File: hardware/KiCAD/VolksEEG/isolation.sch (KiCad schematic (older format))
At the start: 3 parts

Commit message: Added debugging bits to more schematic sheets.
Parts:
- added C? (x5): 100n, symbol Device:C
- added D?: Blue, symbol Device:LED
- added D?: Green, symbol Device:LED
- added R?: 220R, symbol Device:R
- added R?: 330R, symbol Device:R
- added TP? (x3): GNDD_tp, symbol Connector:TestPoint
- added TP?: ADS_nDRDY_tp, symbol Connector:TestPoint
- added TP?: ADS_nDRDY_ni_tp, symbol Connector:TestPoint
- added TP?: MISO_ni_tp, symbol Connector:TestPoint
- added TP?: SCK_tp, symbol Connector:TestPoint
- added TP?: SCK_ni_tp, symbol Connector:TestPoint
- added TP?: nCS_tp, symbol Connector:TestPoint
- added TP?: ADS_nRST_tp, symbol Connector:TestPoint
- added TP?: MOSI_tp, symbol Connector:TestPoint
- added TP?: nCS_ni_tp, symbol Connector:TestPoint
- added TP?: ADS_nRST_ni_tp, symbol Connector:TestPoint
- added TP?: MOSI_ni_tp, symbol Connector:TestPoint
- added TP?: 5V_tp, symbol Connector:TestPoint
- added TP?: MISO_tp, symbol Connector:TestPoint
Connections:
- wire segments 48 -> 96

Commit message: Changed ADuM420 sch symbol to more KiCAD-like look.
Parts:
- removed C? (x2): 100n, symbol Device:C
- removed TP?: ADS_nDRDY_tp, symbol Connector:TestPoint
- removed TP?: ADS_nDRDY_ni_tp, symbol Connector:TestPoint
- removed TP?: MISO_ni_tp, symbol Connector:TestPoint
- removed TP?: MISO_tp, symbol Connector:TestPoint
- removed U? (x2): ADUM240E1BRIZ-RL, RI_16_2_ADI, symbol VolksEEG:ADUM240E1BRIZ-RL
- added C? (x2): 100n, symbol Device:C
- added TP?: ADS_nRST_tp, symbol Connector:TestPoint
- added TP?: MOSI_tp, symbol Connector:TestPoint
- added TP?: ADS_nRST_ni_tp, symbol Connector:TestPoint
- added TP?: MOSI_ni_tp, symbol Connector:TestPoint
- added U? (x2): ADUM240E1BRIZ-RL, RI_16_2_ADI, symbol VolksEEG:ADUM240E1BRIZ-RL
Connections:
- wire segments 96 -> 104
- no-connect marks 0 -> 4
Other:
- moved on the sheet: C?, TP?

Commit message: Changed MEJ1S sch symbol to be more KiCAD-like.
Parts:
- removed U?: MEJ1S0305SC, MEJ1_SINGLE_SIP_MUR, symbol MEJ1S0305SC:MEJ1S0305SC
- added U?: MEJ1S0305SC, MEJ1_SINGLE_SIP_MUR, symbol VolksEEG:MEJ1S0305SC
- C?: symbol Device:C -> Device:C_Small
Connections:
- wire segments 104 -> 106
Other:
- note added: "5V Boost Converter\n(Isolation)"
- moved on the sheet: C?, TP?, U?

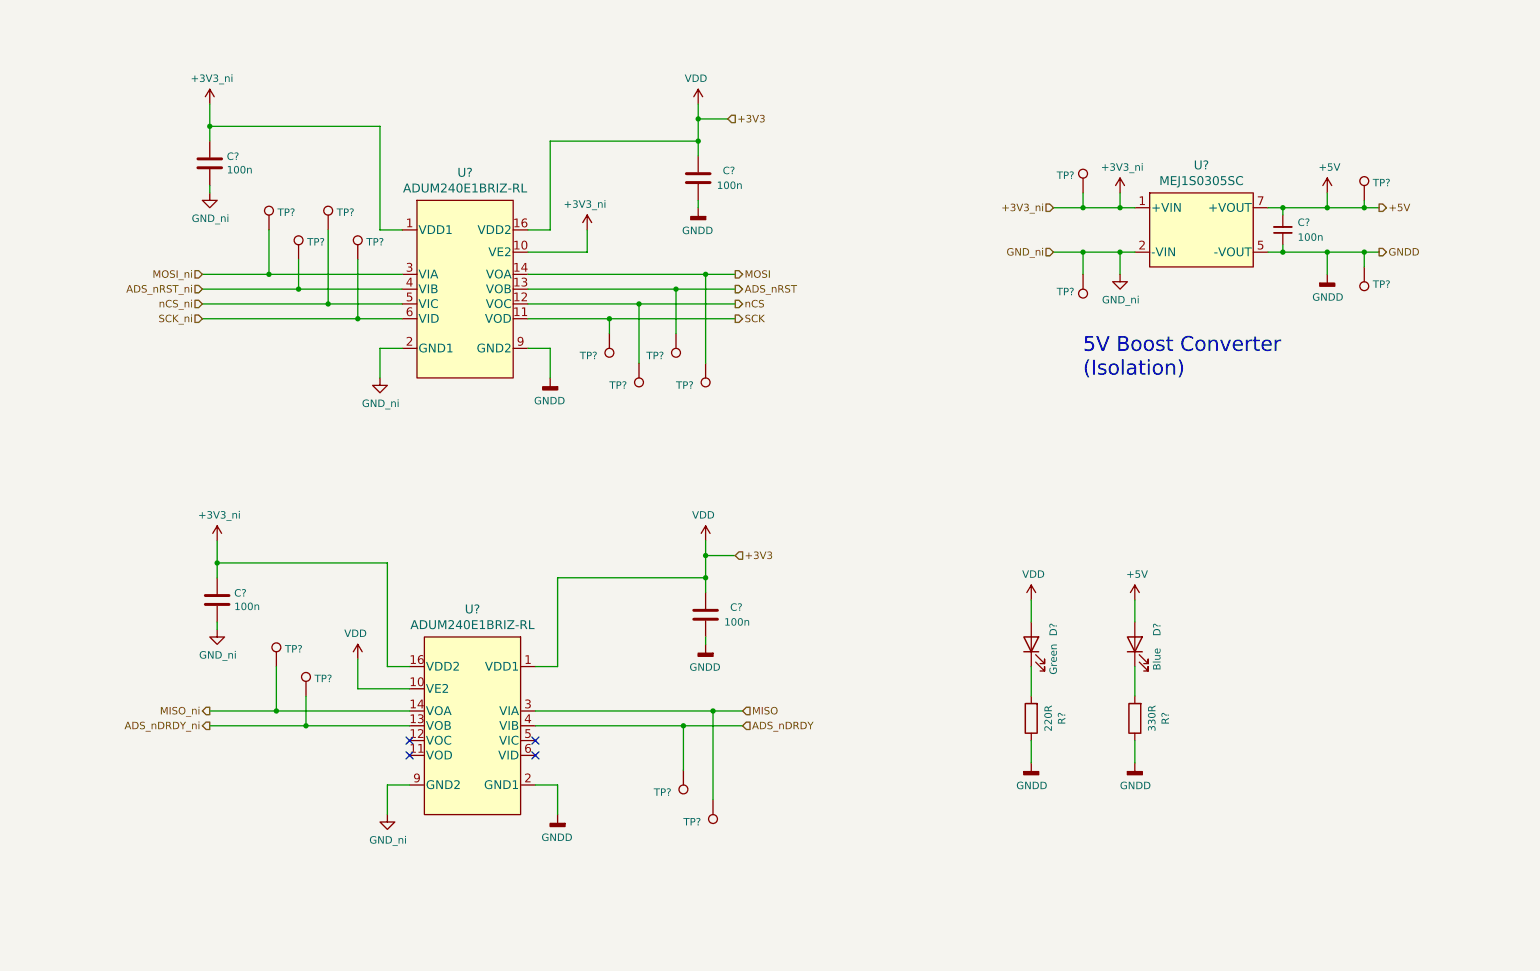
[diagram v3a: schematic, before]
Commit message: Cleaned up nrf page and converted +3V3_ni to non-global symbols.
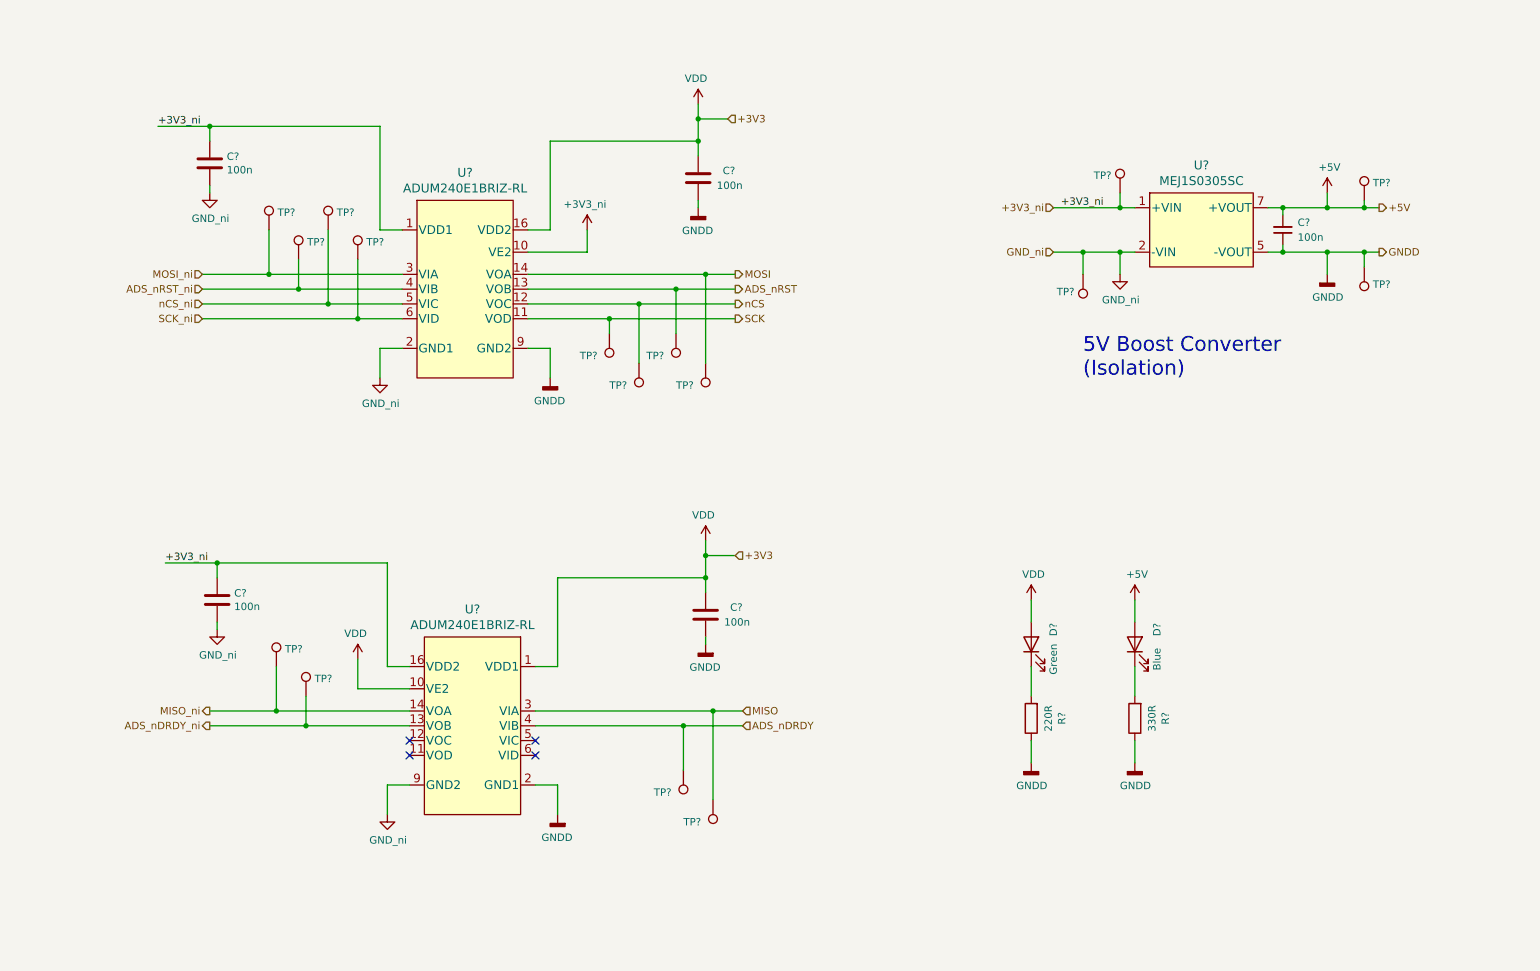
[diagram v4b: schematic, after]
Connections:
- net +3V3: no longer C?.2, C?.2, TP?.1, U?.1 (+VIN), U?.1 (VDD1), U?.16 (VDD2)
- new net +3V3_ni: C?.2, C?.2, TP?.1, U?.1 (+VIN), U?.1 (VDD1), U?.16 (VDD2)
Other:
- moved on the sheet: TP?
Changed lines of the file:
@@
 +3V3
-$Comp
-L VolksEEG:+3V3_ni #PWR?
-U 1 1 61BD5B0A
-P 8200 1900
-F 0 "#PWR?" H 8200 1750 50  0001 C CNN
-F 1 "+3V3_ni" H 8215 2073 50  0000 C CNN
-F 2 "" H 8200 1900 50  0001 C CNN
-F 3 "" H 8200 1900 50  0001 C CNN
-	1    8200 1900
-	1    0    0    -1
-$EndComp
 $Comp
 L VolksEEG:GND_ni #PWR?
@@
 	1    0    0    -1
 $EndComp
-$Comp
-L VolksEEG:+3V3_ni #PWR?
-U 1 1 61BD925C
-P 2050 1300
-F 0 "#PWR?" H 2050 1150 50  0001 C CNN
-F 1 "+3V3_ni" H 2065 1473 50  0000 C CNN
-F 2 "" H 2050 1300 50  0001 C CNN
-F 3 "" H 2050 1300 50  0001 C CNN
-	1    2050 1300
-	1    0    0    -1
-$EndComp
 Wire Wire Line
 	5350 1300 5350 1400
-Wire Wire Line
-	2050 1450 2050 1300
 Wire Wire Line
 	2050 1850 2050 1900
@@
 	5350 1650 5350 1550
 Connection ~ 5350 1550
-Connection ~ 2050 1450
 $Comp
 L Connector:TestPoint TP?
@@
 L Connector:TestPoint TP?
 U 1 1 617B0F77
-P 7950 1900
-F 0 "TP?" H 8008 2018 50  0000 L CNN
-F 1 "GNDD_tp" H 8008 1927 50  0001 L CNN
-F 2 "" H 8150 1900 50  0001 C CNN
-F 3 "~" H 8150 1900 50  0001 C CNN
-	1    7950 1900
+P 8200 1900
+F 0 "TP?" H 8258 2018 50  0000 L CNN
+F 1 "GNDD_tp" H 8258 1927 50  0001 L CNN
+F 2 "" H 8400 1900 50  0001 C CNN
+F 3 "~" H 8400 1900 50  0001 C CNN
+	1    8200 1900
 	-1   0    0    -1
 $EndComp
@@
 $EndComp
 $Comp
-L power:VDD #PWR?
-U 1 1 618CFDA1
-P 7600 4650
-AR Path="/615BA255/618CFDA1" Ref="#PWR?"  Part="1"
-AR Path="/61731DC5/618CFDA1" Ref="#PWR?"  Part="1"
-F 0 "#PWR?" H 7600 4500 50  0001 C CNN
-F 1 "VDD" H 7615 4823 50  0000 C CNN
-F 2 "" H 7600 4650 50  0001 C CNN
-F 3 "" H 7600 4650 50  0001 C CNN
-	1    7600 4650
-	1    0    0    -1
-$EndComp
-$Comp
 L power:+5V #PWR?
 U 1 1 618D0E10
@@
 	1    0    0    -1
 $EndComp
-Wire Wire Line
-	7600 4650 7600 4800
 Wire Wire Line
 	7600 5100 7600 5300
@@
 	1    0    0    -1
 $EndComp
-$Comp
-L VolksEEG:+3V3_ni #PWR?
-U 1 1 61872518
-P 2100 4250
-F 0 "#PWR?" H 2100 4100 50  0001 C CNN
-F 1 "+3V3_ni" H 2115 4423 50  0000 C CNN
-F 2 "" H 2100 4250 50  0001 C CNN
-F 3 "" H 2100 4250 50  0001 C CNN
-	1    2100 4250
-	1    0    0    -1
-$EndComp
 Wire Wire Line
 	5400 4250 5400 4350
-Wire Wire Line
-	2100 4400 2100 4250
 Wire Wire Line
 	2100 4800 2100 4850
@@
 	7750 2300 7950 2300
 Wire Wire Line
-	8300 2000 8200 2000
-Wire Wire Line
-	8200 2000 8200 1900
-Wire Wire Line
-	8200 2000 7950 2000
-Connection ~ 8200 2000
-Wire Wire Line
-	7950 1900 7950 2000
-Connection ~ 7950 2000
-Wire Wire Line
-	7950 2000 7750 2000
+	8200 1900 8200 2000
 Wire Wire Line
 	9600 2300 9600 2450
@@
 Text Notes 7950 3150 0    100  ~ 0
 5V Boost Converter\n(Isolation)
+Wire Wire Line
+	2050 1450 1700 1450
+Connection ~ 2050 1450
+$Comp
+L power:VDD #PWR?
+U 1 1 618CFDA1
+P 7600 4650
+AR Path="/615BA255/618CFDA1" Ref="#PWR?"  Part="1"
+AR Path="/61731DC5/618CFDA1" Ref="#PWR?"  Part="1"
+F 0 "#PWR?" H 7600 4500 50  0001 C CNN
+F 1 "VDD" H 7615 4823 50  0000 C CNN
+F 2 "" H 7600 4650 50  0001 C CNN
+F 3 "" H 7600 4650 50  0001 C CNN
+	1    7600 4650
+	1    0    0    -1
+$EndComp
+Wire Wire Line
+	7600 4650 7600 4800
+Wire Wire Line
+	2100 4400 1750 4400
+Text Label 7800 2000 0    50   ~ 0
++3V3_ni
+Text Label 1750 4400 0    50   ~ 0
++3V3_ni
+Text Label 1700 1450 0    50   ~ 0
++3V3_ni
+Connection ~ 8200 2000
+Wire Wire Line
+	8200 2000 8300 2000
+Wire Wire Line
+	7750 2000 8200 2000
 $EndSCHEMATC

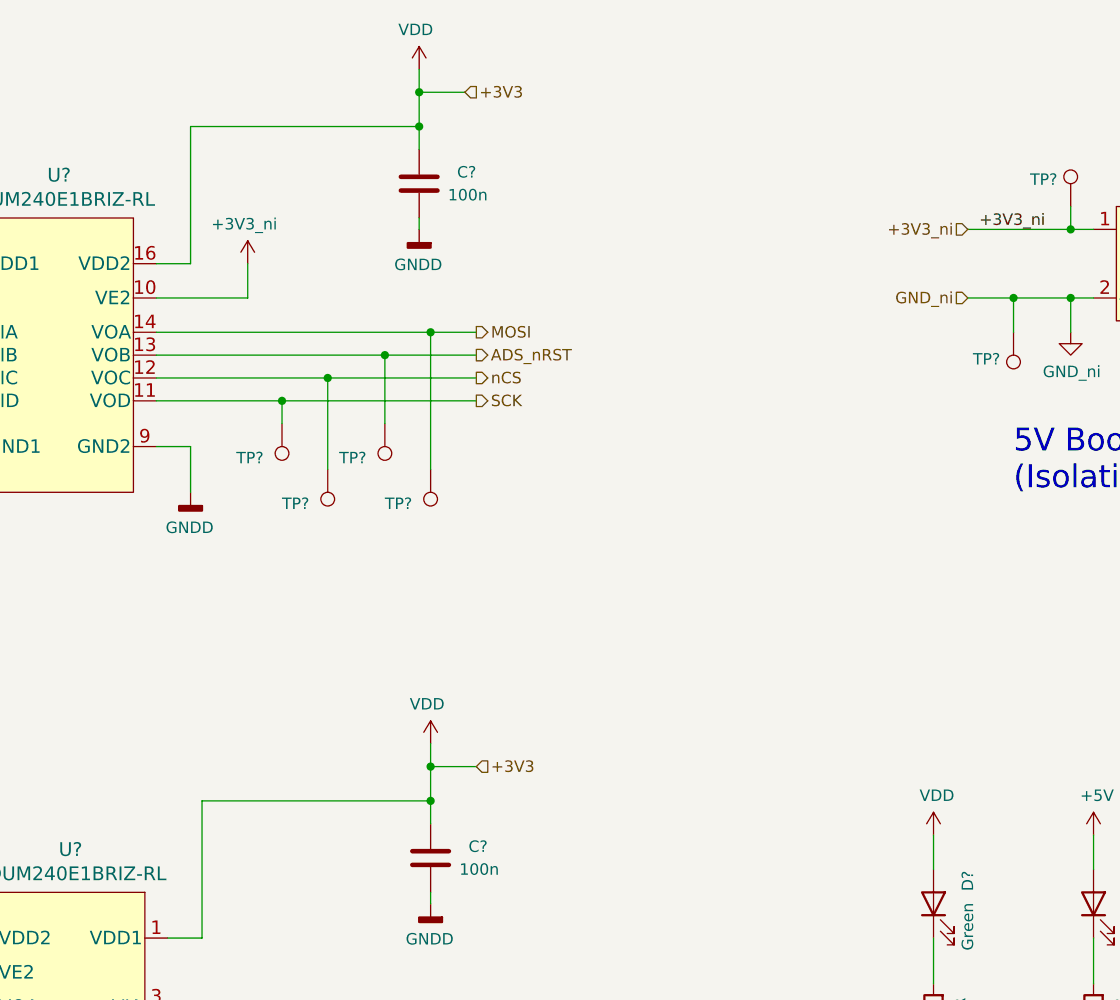
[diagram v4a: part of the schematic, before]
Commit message: Fixed an bug with the global power nets being used.
The use of global power nets caused the +3V3A, +3V3, and -3V3A nets to be shorted together.
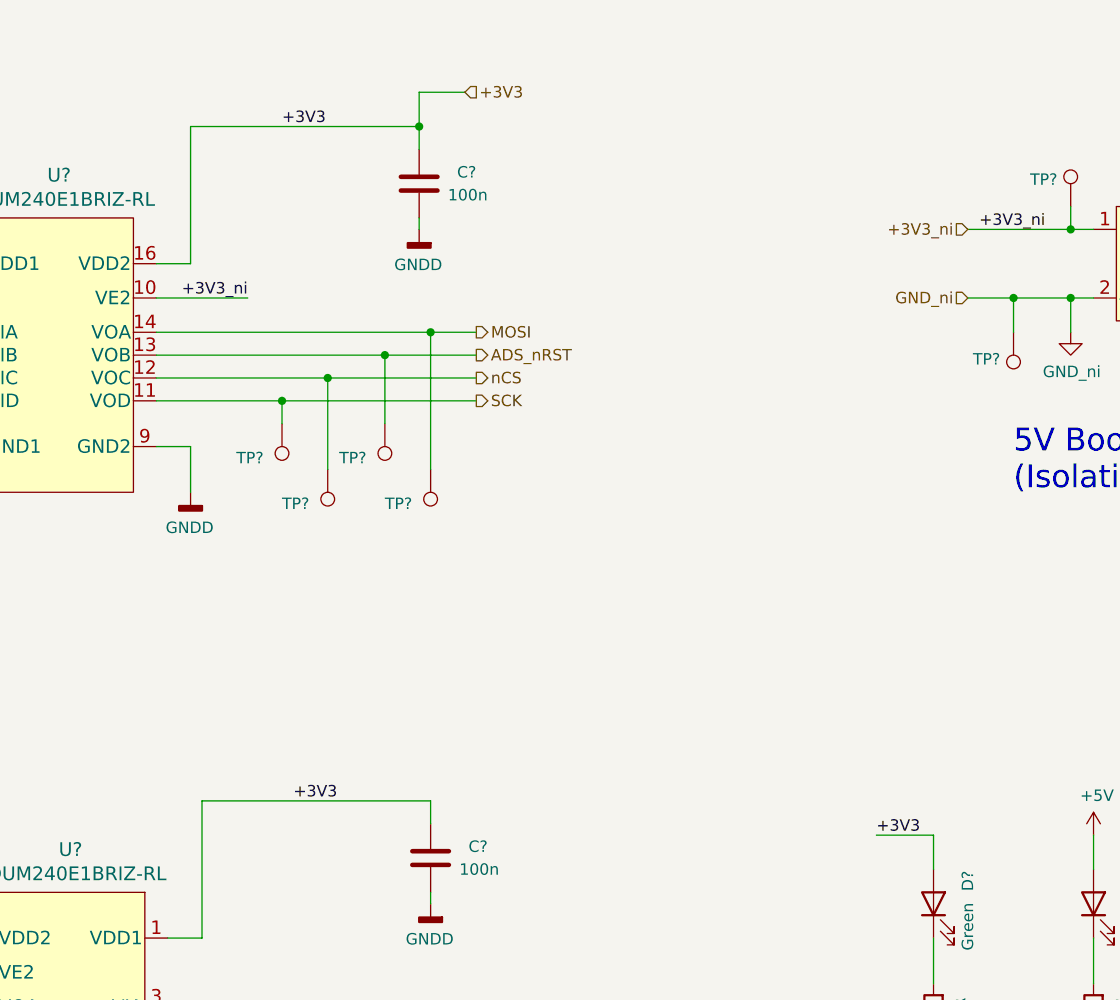
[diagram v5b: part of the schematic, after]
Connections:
- net +3V3: no longer U?.10 (VE2), U?.10 (VE2)
- net +3V3_ni: now also U?.10 (VE2)
- new net VDD: U?.10 (VE2)

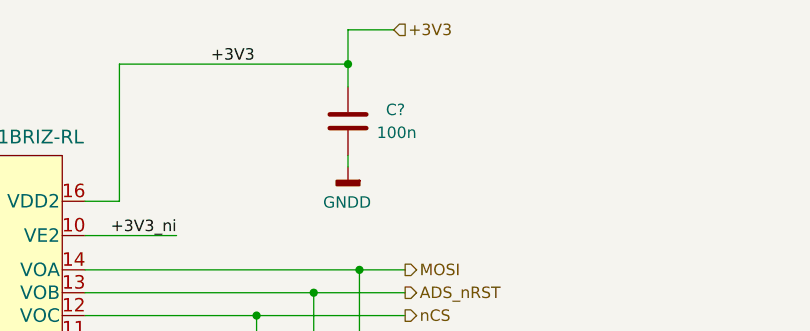
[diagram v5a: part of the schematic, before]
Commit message: Removed custom global power symbols to prevent the bug from happening again.
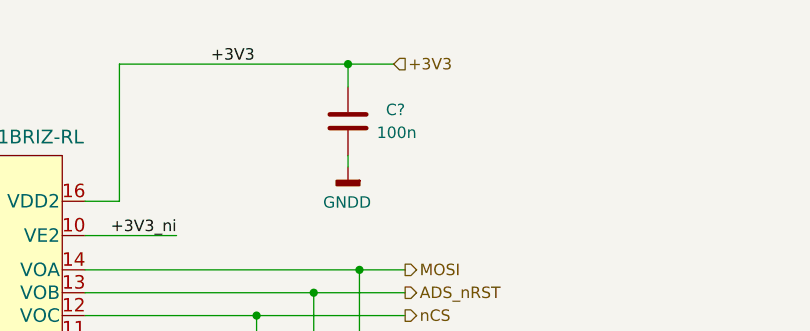
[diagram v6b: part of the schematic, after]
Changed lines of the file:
@@
 Text HLabel 9950 2000 2    50   Output ~ 0
 +5V
-Text HLabel 5550 1400 2    50   Input ~ 0
+Text HLabel 5550 1550 2    50   Input ~ 0
 +3V3
 $Comp
@@
 	2000 2750 3050 2750
 Wire Wire Line
-	5550 1400 5350 1400
-Wire Wire Line
-	5350 1400 5350 1550
+	5550 1550 5350 1550
 $Comp
 L Device:C C?
